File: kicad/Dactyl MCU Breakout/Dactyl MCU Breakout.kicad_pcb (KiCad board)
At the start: 2 copper layers, 63 x 58 mm, 35 parts, among them J1 Columns, J2 Rows, J3 Thumbs, J5 Display, J6 External, J7 JST, J8 Split, J9 Vic, K1 Key, SW1 Battery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

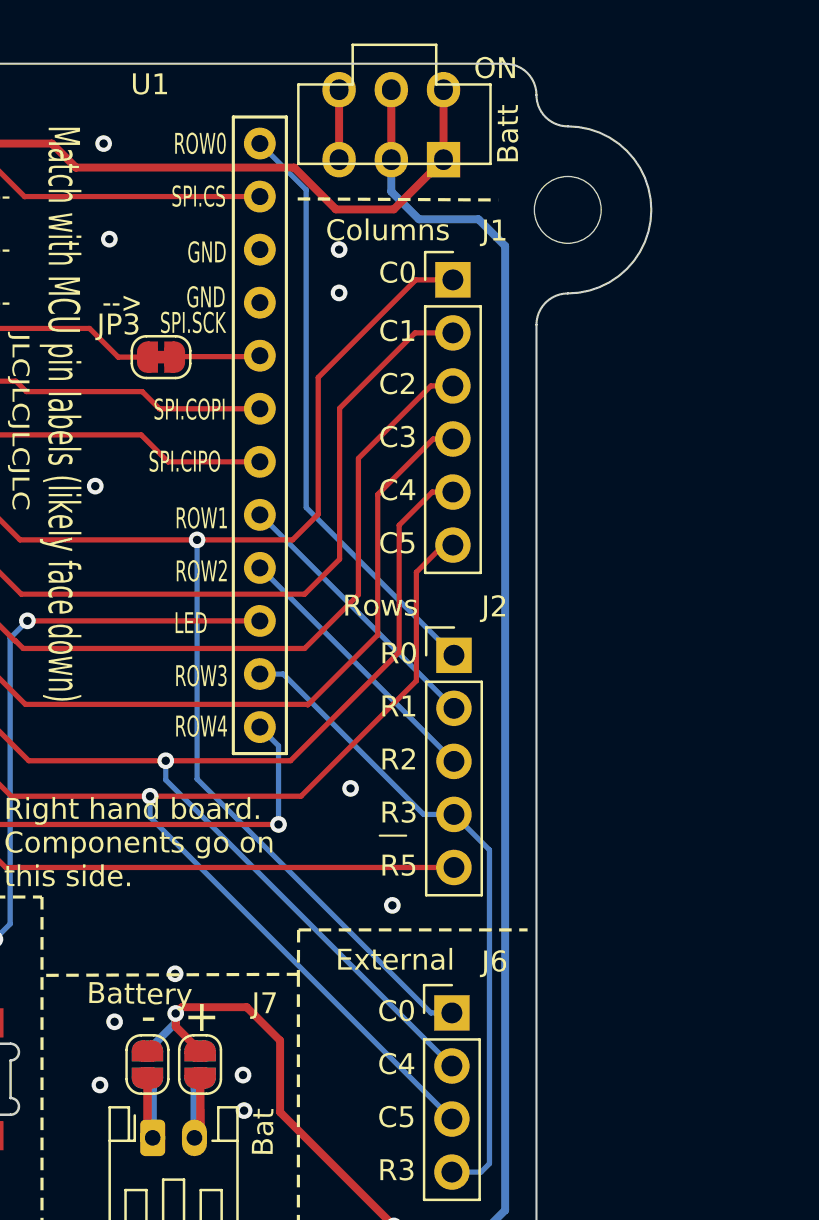
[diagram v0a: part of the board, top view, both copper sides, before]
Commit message: feat(pcb): mount point further from bat swittch
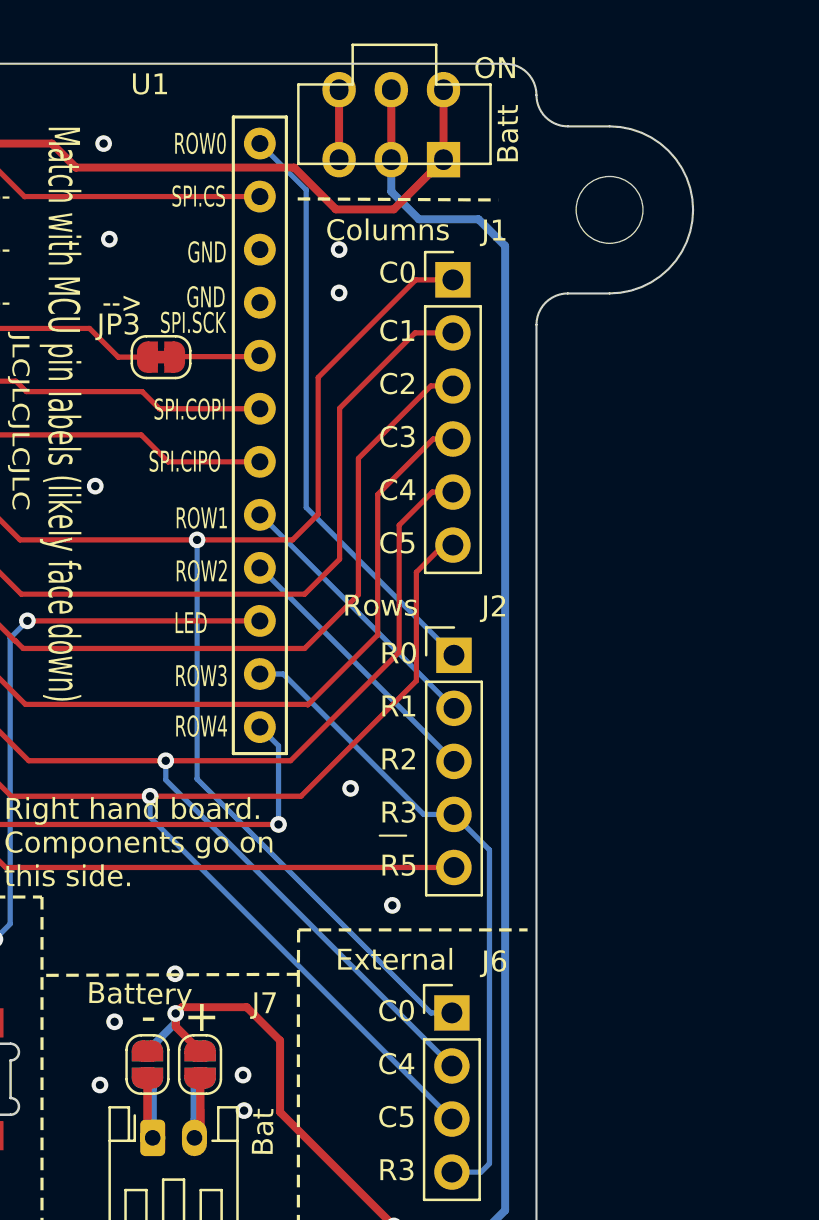
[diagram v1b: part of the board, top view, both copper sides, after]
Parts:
- moved H1 2.00 mm to (155.5, 57.0)
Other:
- board size 63 x 58 mm -> 65 x 58 mm
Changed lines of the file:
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@@
 		(fp_arc
 			(start 6.938123 15.132041)
-			(mid 6.337066 14.8831)
+			(mid 6.337062 14.8831)
 			(end 6.088123 14.282041)
 			(stroke
@@
 		(fp_arc
 			(start 8.236041 -15.740877)
-			(mid 8.837089 -15.491924)
+			(mid 8.837086 -15.491923)
 			(end 9.086041 -14.890877)
 			(stroke
@@
 		(fp_arc
 			(start 1.550062 2.100001)
-			(mid 2.045036 2.305028)
+			(mid 2.045039 2.305027)
 			(end 2.250063 2.800003)
 			(stroke
@@
 		(fp_arc
 			(start 1.551371 2.100001)
-			(mid 2.046344 2.305026)
+			(mid 2.046348 2.305026)
 			(end 2.251372 2.8)
 			(stroke
@@
 	(footprint "MountingHole:MountingHole_3.2mm_M3_DIN965"
 		(layer "F.Cu")
-		(at 153.5 57)
+		(at 155.5 57)
 		(descr "Mounting Hole 3.2mm, no annular, M3, DIN965")
 		(tags "mounting hole 3.2mm no annular m3 din965")
@@
 	)
 	(gr_line
+		(start 151.5 57)
+		(end 151.5 49.15)
+		(stroke
+			(width 0.1)
+			(type default)
+		)
+		(layer "Dwgs.User")
+	)
+	(gr_arc
+		(start 155.5 61)
+		(mid 151.5 57)
+		(end 155.5 53)
+		(stroke
+			(width 0.1)
+			(type default)
+		)
+		(layer "Dwgs.User")
+	)
+	(gr_line
 		(start 100 98.5)
 		(end 100 51.5)
@@
 		(layer "Edge.Cuts")
 	)
+	(gr_line
+		(start 153.5 53)
+		(end 155.5 53)
+		(stroke
+			(width 0.1)
+			(type default)
+		)
+		(layer "Edge.Cuts")
+	)
 	(gr_arc
 		(start 152 62.5)
@@
 		(layer "Edge.Cuts")
 	)
+	(gr_line
+		(start 153.5 61)
+		(end 155.5 61)
+		(stroke
+			(width 0.1)
+			(type default)
+		)
+		(layer "Edge.Cuts")
+	)
 	(gr_arc
 		(start 100 98.5)
@@
 	)
 	(gr_arc
-		(start 153.5 53)
-		(mid 157.5 57)
-		(end 153.5 61)
+		(start 155.5 53)
+		(mid 159.5 57)
+		(end 155.5 61)
 		(stroke
 			(width 0.1)

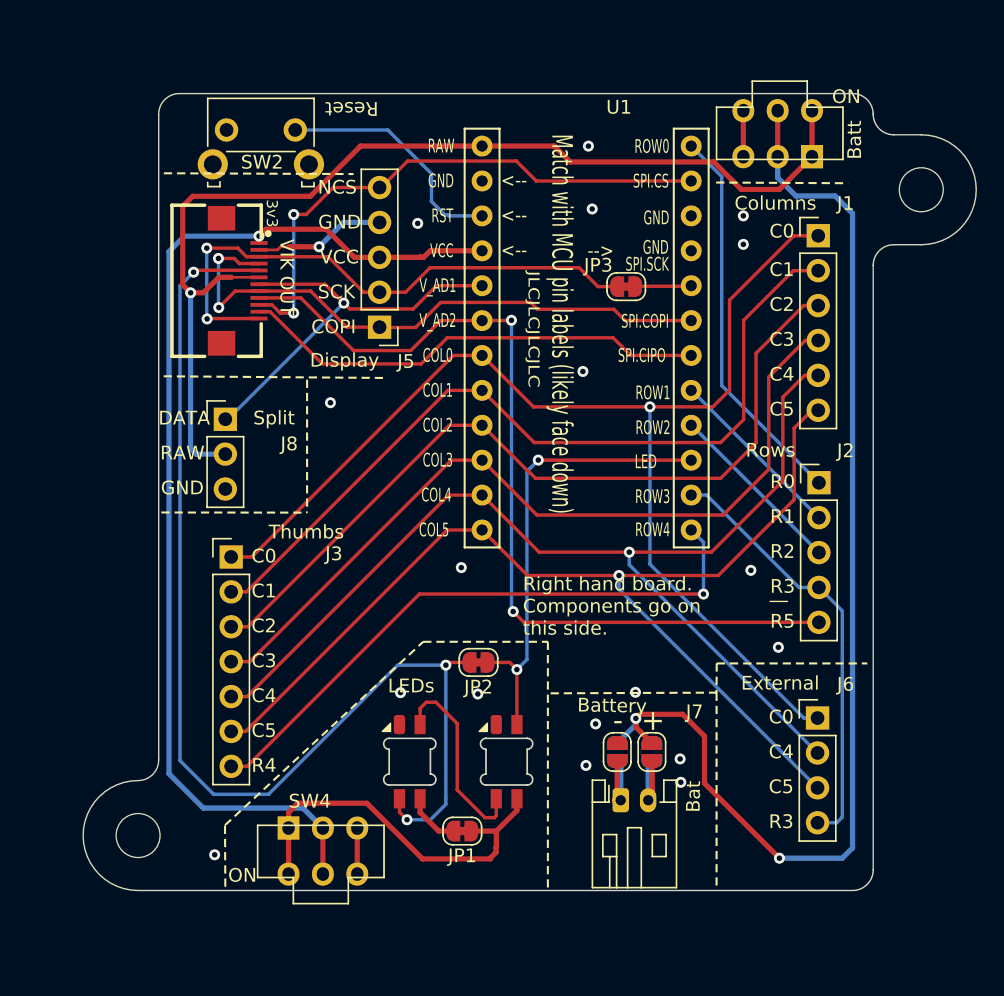
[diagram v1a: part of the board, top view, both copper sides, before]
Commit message: feat: area reserved for TRRS. base plate notch
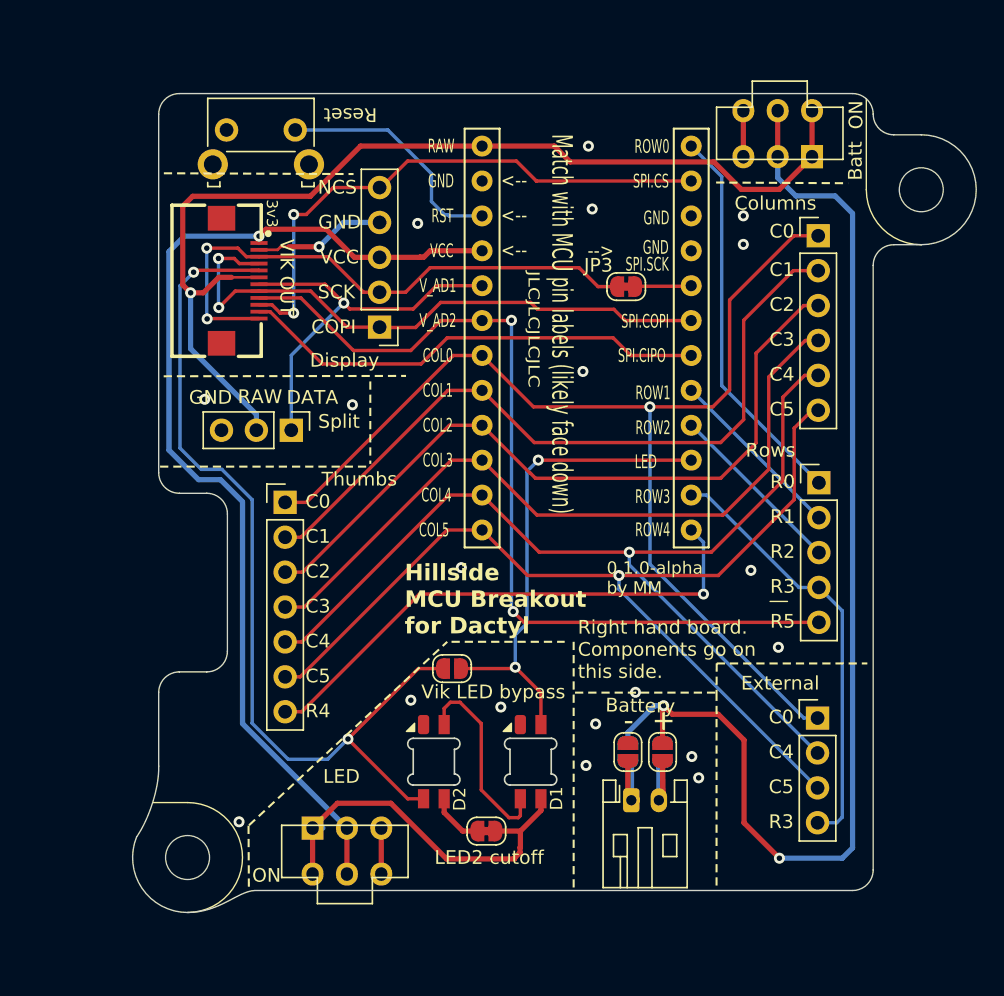
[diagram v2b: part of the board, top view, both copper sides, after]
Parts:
- added K1: Key, Dactyl:pg1350, B.Cu at (258.3, 74.1)
- added K1: Key, Dactyl:pg1350, B.Cu at (276.3, 74.1)
- added K1: Key, Dactyl:pg1350, B.Cu at (258.3, 108.1)
- added K1: Key, Dactyl:pg1350, B.Cu at (71.3, 140.9)
- added K1: Key, Dactyl:pg1350, B.Cu at (258.3, 91.1)
- added K1: Key, Dactyl:pg1350, B.Cu at (107.3, 141.1)
- added K1: Key, Dactyl:pg1350, B.Cu at (276.3, 91.1)
- added K1: Key, Dactyl:pg1350, B.Cu at (276.3, 108.1)
- added K1: Key, Dactyl:pg1350, B.Cu at (89.3, 140.9)
- JP2: value LEDs bypass -> Vik LED bypass; footprint Jumper:SolderJumper-2_P1.3mm_Bridged_RoundedPad1.0x1.5mm -> Jumper:SolderJumper-2_P1.3mm_Open_RoundedPad1.0x1.5mm
- moved K1 257.6 mm to (222.2, 85.2)
- moved K1 257.6 mm to (204.2, 91.5)
- moved K1 257.6 mm to (204.2, 108.5)
- moved K1 257.6 mm to (240.2, 83.7)
- moved K1 257.6 mm to (222.2, 68.2)
- moved K1 257.6 mm to (186.2, 108.5)
- moved K1 257.6 mm to (204.2, 74.5)
- moved K1 257.6 mm to (186.2, 74.5)
- moved K1 257.6 mm to (240.2, 117.7)
- moved K1 257.6 mm to (240.2, 66.7)
- moved K1 257.6 mm to (222.2, 119.2)
- moved K1 257.6 mm to (186.2, 91.5)
- moved K1 257.6 mm to (240.2, 100.7)
- moved K1 257.6 mm to (222.2, 102.2)
- moved K1 170.1 mm to (71.3, 123.8)
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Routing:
- net /Right/LED_out: track 82.1 -> 66.3 mm, vias 3 -> 2
- net /Right/col5: track 79.6 -> 74.1 mm
- net /Right/row4: track 44.6 -> 39.0 mm
- net /Right/col4: track 79.7 -> 74.1 mm
- net /Right/col2: track 59.4 -> 53.9 mm
- net /Right/col0: track 87.6 -> 82.1 mm
- net /Right/col1: track 59.8 -> 54.2 mm
- net /Right/col3: track 59.7 -> 54.1 mm
- net /Right/VCC: track 75.8 -> 73.2 mm
- net /Right/LED: track 33.4 -> 35.8 mm
- net /Right/RAW: track 75.9 -> 73.9 mm
- net /Right/bat+: track 81.4 -> 83.4 mm
- net /Right/SPLIT_VIK_GP_AD1: track 30.1 -> 28.5 mm
- net /Right/VCC_LED1: track 24.8 -> 24.1 mm
- net GND: vias 19 -> 20
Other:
- board size 65 x 58 mm -> 61.4 x 59.6 mm
- board text added: "${REVISION} by MM"
- board text added: "Hillside MCU Breakout for Dactyl"
- board text added: "TRRS fits in split area"
- board text removed: "LEDs"

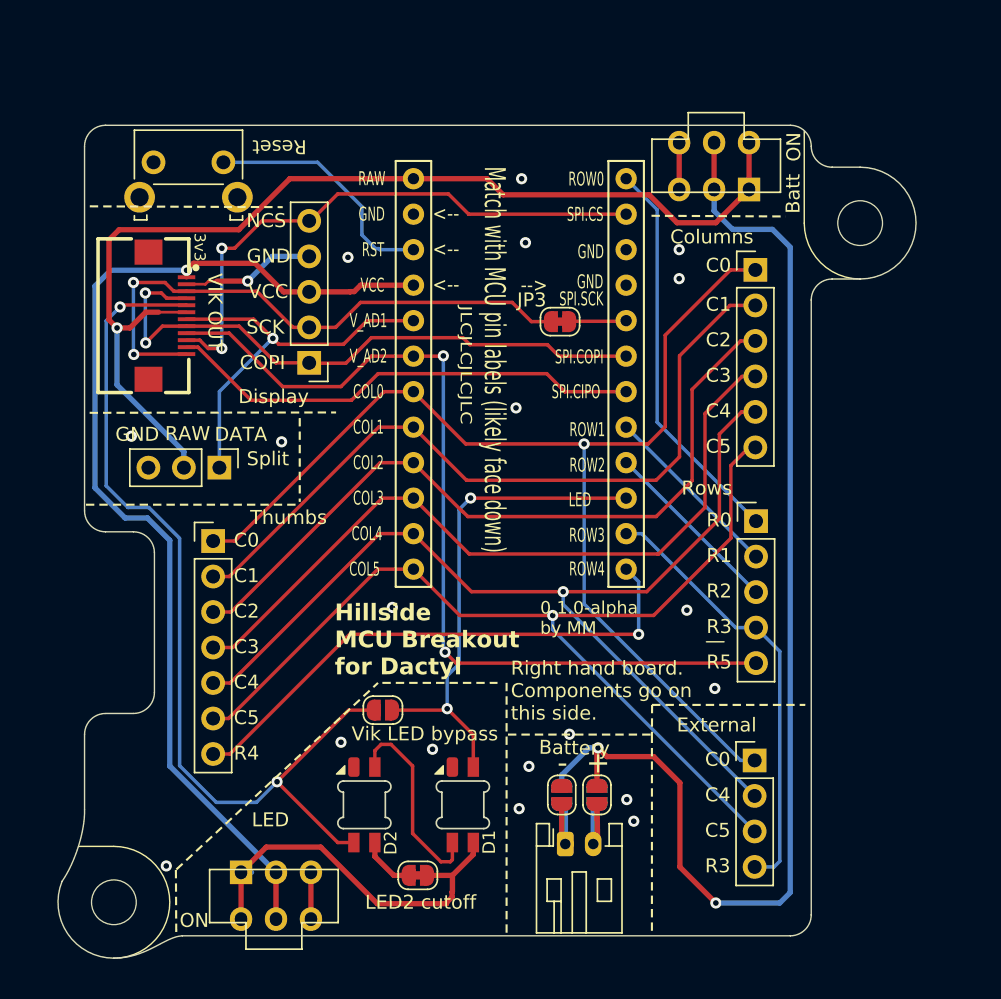
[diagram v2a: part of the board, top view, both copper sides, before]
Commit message: feat: left: reset and batt, right: two inserts
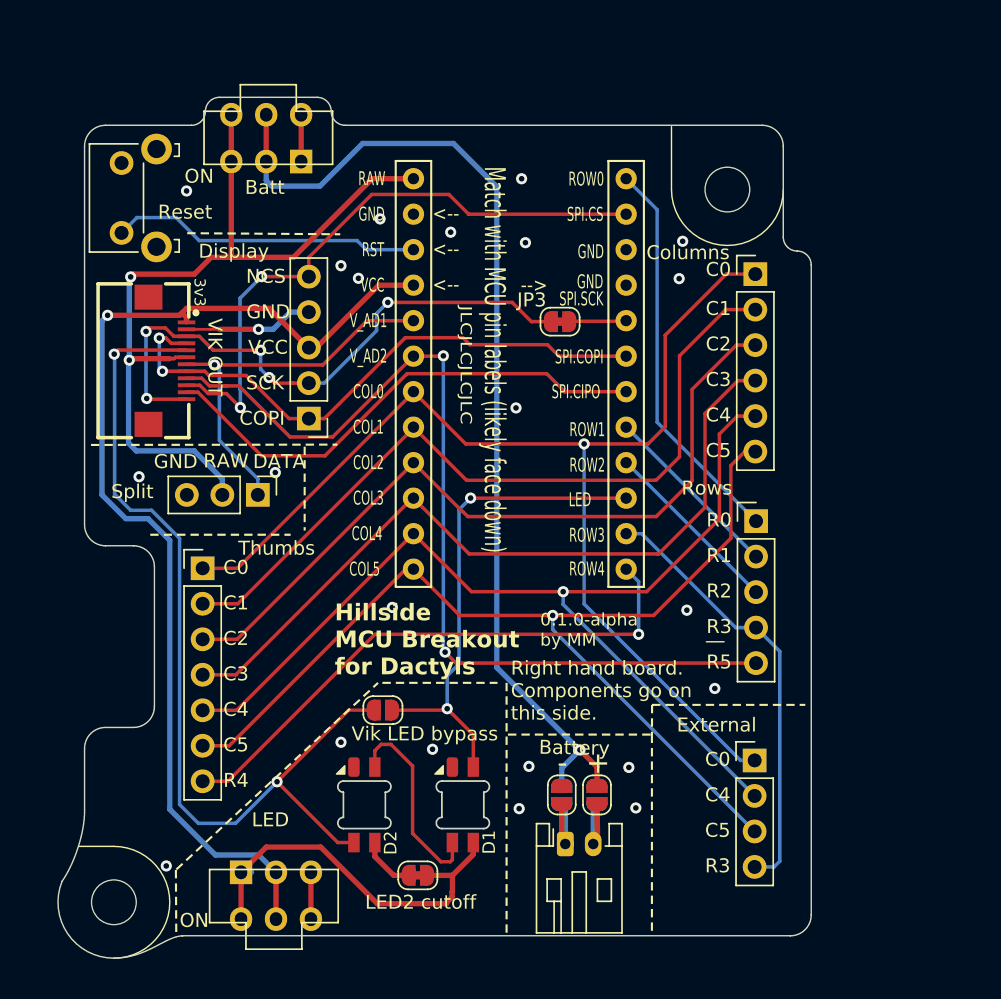
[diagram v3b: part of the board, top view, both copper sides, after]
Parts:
- moved SW1 32.1 mm to (113.0, 50.9)
- moved H1 9.80 mm to (146.0, 54.6), turned to -90 degrees
- moved J5 3.99 mm to (116.0, 71.0)
- moved SW2 3.77 mm to (103.9, 55.2), turned to -90 degrees
- moved J8 3.37 mm to (112.4, 76.5)
- moved J9 3.22 mm to (105.3, 66.8)
- moved J3 2.09 mm to (108.5, 81.7)
- moved J1 0.30 mm to (148.0, 60.6)
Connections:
- SW1 pad 1: /Right/RAW -> unconnected-(SW1-A-Pad1)
- SW1 pad 3: unconnected-(SW1-C-Pad3)_0 -> /Right/RAW
- SW2 pad 1: /Right/RST -> GND
- SW2 pad 2: GND -> /Right/RST
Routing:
- net /Right/RAW: track 73.9 -> 55.1 mm, vias 1 -> 2
- net /Right/bat+: track 83.4 -> 69.5 mm, vias 2 -> 1
- net /Right/RST: track 17.4 -> 22.3 mm
- net /Right/SPI0.SC: track 41.1 -> 44.4 mm
- net /Right/SPI0.CIPO: track 34.4 -> 36.3 mm
- net /Right/SPI0.COPI/SCL: track 44.0 -> 42.1 mm
- net /Right/row5_VIK_GP_AD2: track 64.7 -> 66.5 mm
- net /Right/row4: track 39.0 -> 40.6 mm
- net /Right/col1: track 54.2 -> 55.7 mm
- net /Right/col0: track 82.1 -> 83.5 mm
- net /Right/col2: track 53.9 -> 55.3 mm
- net /Right/col5: track 74.1 -> 75.5 mm
- net /Right/col3: track 54.1 -> 55.5 mm
- net /Right/col4: track 74.1 -> 75.6 mm
- net /Right/SPI0.SCK/SDA: track 41.5 -> 42.9 mm, vias 2 -> 5
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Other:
- board size 61.4 x 59.6 mm -> 53.9 x 61.6 mm
- board text added: "Hillside MCU Breakout for Dactyls"
- board text removed: "Hillside MCU Breakout for Dactyl"
